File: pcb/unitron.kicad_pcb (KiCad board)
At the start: 2 copper layers, 80.5 x 141 mm, 69 parts, among them J1 Conn_01x09_Female, J2 Conn_01x09_Male, J3 Conn_01x09_Female, J4 Conn_01x09_Male, J5 Conn_02x03_Odd_Even, Q1 FDN340P, Q2 BSS123, SW1 SW_SPST, U1 LTC-4727JS, U2 LTC-4727JS, U3 AS1115-BSST, U4 ATSAMD21E, U5 LTC-4727JR, U6 LTC-4727JR, U7 AS1115-BSST

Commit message: PCB v1.5
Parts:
- removed D14: LED, LED_SMD:LED_0805_2012Metric
- removed MB1, MB2, MB3: VAL**, asl_footprints:mouse-bite-2.54mm-slot-long
- removed R2: 10KΩ, Resistor_SMD:R_0805_2012Metric
- added MB*: VAL**, asl_footprints:mouse-bite-2.54mm-slot-long, F.Cu at (72.5, 66.1)
- added MB*: VAL**, asl_footprints:mouse-bite-2.54mm-slot-long, F.Cu at (105.1, 66.1)
- added MB*: VAL**, asl_footprints:mouse-bite-2.54mm-slot-long, F.Cu at (137.4, 66.1)
- added S16: Gateron Blue, Button_Switch_Keyboard:SW_Cherry_MX_1.00u_PCB, F.Cu at (98.0, 155.2)
- added U8: AT24C01C-STUM, Package_TO_SOT_SMD:SOT-23-5, B.Cu at (121.9, 71.4)
- BT1: value 2466 -> 2468
- D1, D10, D11, D12, D2, D3, D4, D5, D6, D7, D8, D9: footprint LED_SMD:LED-APA102-2020 -> asl_footprints:LED-APA102-2020
- J1, J3: footprint Connector_PinSocket_2.54mm:PinSocket_1x09_P2.54mm_Vertical -> Connector_PinSocket_2.54mm:PinSocket_1x09_P2.54mm_Vertical_SMD_Pin1Left
- S4: footprint Button_Switch_Keyboard:SW_Cherry_MX_2.00u_PCB -> Button_Switch_Keyboard:SW_Cherry_MX_1.00u_PCB
- SW1: footprint asl_footprints:B12AP -> asl_footprints:switch_nkk_reinforced_pc_pin
- moved S4 87.4 mm to (79.0, 155.2)
- moved D10 85.4 mm to (109.6, 62.4)
- moved D11 85.4 mm to (124.0, 62.4)
- moved D12 85.4 mm to (138.3, 62.4)
- moved D4 85.4 mm to (109.6, 58.5)
- moved D5 85.4 mm to (124.0, 58.5)
- moved D6 85.4 mm to (138.3, 58.5)
- moved D1 85.4 mm to (66.6, 58.5)
- moved D2 85.4 mm to (80.9, 58.5)
- moved D7 85.4 mm to (66.6, 62.4)
- moved D8 85.4 mm to (80.9, 62.4)
- moved D3 85.4 mm to (95.3, 58.5)
- moved D9 85.4 mm to (95.3, 62.4)
- moved J3 80.9 mm to (142.2, 50.5)
- moved S15 79.5 mm to (128.3, 103.1)
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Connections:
- BT1 pad 2: (no net) -> GND
- C2 pad 2: (no net) -> GND
- D1 pad 2: (no net) -> Net-(D1-Pad2)
- D1 pad 3: (no net) -> Net-(D1-Pad3)
- D12 pad 4: /SDI -> Net-(D12-Pad4)
- D12 pad 5: /CKI -> Net-(D12-Pad5)
- D3 pad 4: Net-(D3-Pad4) -> Net-(D10-Pad3)
- D3 pad 5: Net-(D3-Pad5) -> Net-(D10-Pad2)
- D4 pad 2: Net-(D4-Pad2) -> Net-(D10-Pad5)
- D4 pad 3: Net-(D4-Pad3) -> Net-(D10-Pad4)
- D4 pad 4: Net-(D10-Pad3) -> Net-(D11-Pad3)
- D4 pad 5: Net-(D10-Pad2) -> Net-(D11-Pad2)
- D5 pad 2: Net-(D10-Pad5) -> Net-(D11-Pad5)
- D5 pad 3: Net-(D10-Pad4) -> Net-(D11-Pad4)
- D5 pad 4: Net-(D11-Pad3) -> Net-(D12-Pad3)
- D5 pad 5: Net-(D11-Pad2) -> Net-(D12-Pad2)
- D6 pad 2: Net-(D11-Pad5) -> Net-(D12-Pad5)
- D6 pad 3: Net-(D11-Pad4) -> Net-(D12-Pad4)
- D6 pad 4: Net-(D12-Pad3) -> /CKI
- D6 pad 5: Net-(D12-Pad2) -> /SDI
- D7 pad 2: Net-(D1-Pad5) -> (no net)
- D7 pad 3: Net-(D1-Pad4) -> (no net)
- D7 pad 4: Net-(D2-Pad3) -> Net-(D1-Pad3)
- D7 pad 5: Net-(D2-Pad2) -> Net-(D1-Pad2)
- D8 pad 2: Net-(D2-Pad5) -> Net-(D1-Pad5)
- D8 pad 3: Net-(D2-Pad4) -> Net-(D1-Pad4)
- D8 pad 4: Net-(D3-Pad3) -> Net-(D2-Pad3)
- D8 pad 5: Net-(D3-Pad2) -> Net-(D2-Pad2)
- D9 pad 2: Net-(D3-Pad5) -> Net-(D2-Pad5)
- D9 pad 3: Net-(D3-Pad4) -> Net-(D2-Pad4)
- D9 pad 4: Net-(D4-Pad3) -> Net-(D3-Pad3)
- D9 pad 5: Net-(D4-Pad2) -> Net-(D3-Pad2)
- J3 pad 1: /CKI -> /GND_daughter
- J3 pad 2: /SDI -> /VIN_daughter
- J3 pad 3: /GND_daughter -> /SCL
- J3 pad 4: /VIN_daughter -> /SDA
- J3 pad 5: /SCL -> Net-(J3-Pad5)
- J3 pad 6: /SDA -> Net-(J3-Pad6)
- J3 pad 7: Net-(J3-Pad7) -> /IRQ
- J3 pad 8: Net-(J3-Pad8) -> /CKI
- J3 pad 9: /IRQ -> /SDI
- J4 pad 1: /SCK -> GND
- J4 pad 2: /MOSI -> /VIN
- J4 pad 3: GND -> /SCL_mcu
- J4 pad 4: /VIN -> /SDA_mcu
- J4 pad 5: /SCL_mcu -> /KEYA
- J4 pad 6: /SDA_mcu -> /KEYB
- J4 pad 7: /KEYA -> /IRQ_mcu
- J4 pad 8: /KEYB -> /SCK
- J4 pad 9: /IRQ_mcu -> /MOSI
- U3 pad 11: Net-(J3-Pad7) -> Net-(J3-Pad5)
- U3 pad 12: Net-(J3-Pad8) -> Net-(J3-Pad6)
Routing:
- net /GND_daughter: track 92.4 -> 18.6 mm, vias 14 -> 8
- net Net-(J2-Pad7): track 57.8 -> 98.3 mm
- net Net-(J3-Pad5): track 0.00 -> 40.1 mm, vias 0 -> 2
- net Net-(J3-Pad6): track 0.00 -> 38.8 mm, vias 0 -> 2
- net /VIN_daughter: track 232.5 -> 194.7 mm, vias 5 -> 3
- net Net-(J3-Pad8): track 37.6 -> 0.00 mm, vias 2 -> 0
- net Net-(J3-Pad7): track 37.0 -> 0.00 mm, vias 1 -> 0
- net Net-(D14-Pad2): track 29.6 -> 0.00 mm, vias 1 -> 0
- net Net-(D4-Pad2): track 14.8 -> 0.00 mm
- net Net-(D4-Pad3): track 14.4 -> 0.00 mm
- net /SCK: track 47.8 -> 59.0 mm, vias 1 -> 3
- net /KEYA: track 149.4 -> 160.5 mm
- net Net-(D3-Pad3): track 14.5 -> 4.73 mm
- net Net-(D3-Pad2): track 14.8 -> 5.19 mm
- net Net-(D10-Pad4): track 14.2 -> 4.68 mm
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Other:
- board size 80.5 x 141 mm -> 80.5 x 139 mm
- board text added: "Unitron v1.5"
- board text removed: "Unitron v1.4"

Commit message: pcb v1.6
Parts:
- removed the D11 at (124.0, 62.4)
- removed D12: APA102-2020, asl_footprints:LED-APA102-2020
- added G***: LOGO, LOGO, F.Cu at (89.7, 52.0)
- added G***: LOGO, LOGO, F.Cu at (137.5, 57.8)
- added G***: LOGO, LOGO, F.Cu at (121.5, 57.8)
- added G***: LOGO, LOGO, F.Cu at (103.9, 57.8)
- added G***: LOGO, LOGO, F.Cu at (89.7, 57.8)
- added G***: LOGO, LOGO, F.Cu at (71.1, 52.1)
- added G***: LOGO, LOGO, F.Cu at (71.1, 57.8)
- added G***: LOGO, LOGO, F.Cu at (137.5, 52.0)
- added G***: LOGO, LOGO, F.Cu at (103.9, 52.0)
- added G***: LOGO, LOGO, F.Cu at (121.5, 52.0)
- added R7: 10KΩ, Resistor_SMD:R_0805_2012Metric, B.Cu at (121.5, 94.2)
- added R8: 10KΩ, Resistor_SMD:R_0805_2012Metric, B.Cu at (118.9, 94.2)
- added U1: AP2112K-3.3, Package_TO_SOT_SMD:SOT-23-5, B.Cu at (134.4, 96.6)
- BT1: footprint Battery:BatteryHolder_Keystone_2468_2xAAA -> Battery:BatteryHolder_Keystone_2479_3xAAA
- C2, C3: value 0.1µF -> 100nF
- D1, D10, D2, D3, D4, D5, D6, D7, D8, D9: value APA102-2020 -> SK9822; footprint asl_footprints:LED-APA102-2020 -> asl_footprints:LED_SK9822_5050
- J1, J3: value Conn_01x09_Female -> Conn_01x10_Male; footprint Connector_PinSocket_2.54mm:PinSocket_1x09_P2.54mm_Vertical_SMD_Pin1Left -> Connector_PinSocket_2.54mm:PinSocket_1x10_P2.54mm_Vertical_SMD_Pin1Right
- J2, J4: value Conn_01x09_Male -> Conn_01x10_Female; footprint Connector_PinHeader_2.54mm:PinHeader_1x09_P2.54mm_Vertical -> Connector_PinHeader_2.54mm:PinHeader_1x10_P2.54mm_Vertical
- moved D6 70.7 mm to (67.6, 57.8), turned to 180 degrees
- moved BT1 26.9 mm to (128.2, 94.2)
- moved D10 24.8 mm to (134.0, 57.8), turned to 180 degrees
- moved D9 23.2 mm to (118.0, 57.8), turned to 180 degrees
- moved D7 20.2 mm to (86.2, 57.8), turned to 180 degrees
- moved D8 20.0 mm to (100.4, 57.8), turned to 180 degrees
- moved D5 12.0 mm to (134.0, 52.0), turned to 180 degrees
- moved D4 10.7 mm to (118.0, 52.0), turned to 180 degrees
- moved H3 9.15 mm to (135.6, 158.0)
- moved U3 8.91 mm to (124.2, 41.4)
- moved U8 8.91 mm to (124.2, 28.3)
- moved R13 8.91 mm to (106.7, 33.4)
- moved R4 8.91 mm to (112.4, 45.6)
- moved R5 8.91 mm to (106.8, 46.1)
- moved R6 8.91 mm to (110.1, 44.5)
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- renumbered D13 to D11, R9 to R10, R10 to R11, R11 to R12, R12 to R13, R13 to R14, R14 to R15, R3 to R2, R4 to R3, R5 to R4, R6 to R5, R7 to R6, R8 to R9, S9 to S10, S10 to S11, S11 to S12, S12 to S13, S13 to S14, S14 to S15, S15 to S16, S16 to S7, S7 to S8, S8 to S9, U1 to U2, U2 to U3, U3 to U4, U4 to U5, U8 to U6, U5 to U7, U6 to U8, U7 to U9
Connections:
- D1 pad 1: /VIN_daughter -> Net-(D1-Pad1)
- D1 pad 3: Net-(D1-Pad3) -> /GND_daughter
- D1 pad 4: Net-(D1-Pad4) -> /VIN_daughter
- D1 pad 6: /GND_daughter -> Net-(D1-Pad6)
- D10 pad 1: /VIN_daughter -> Net-(D10-Pad1)
- D10 pad 3: Net-(D10-Pad3) -> /GND_daughter
- D10 pad 4: Net-(D10-Pad4) -> /VIN_daughter
- D10 pad 6: /GND_daughter -> Net-(D10-Pad6)
- D2 pad 1: /VIN_daughter -> Net-(D2-Pad1)
- D2 pad 3: Net-(D2-Pad3) -> /GND_daughter
- D2 pad 4: Net-(D2-Pad4) -> /VIN_daughter
- D2 pad 6: /GND_daughter -> Net-(D2-Pad6)
- D3 pad 1: /VIN_daughter -> Net-(D3-Pad1)
- D3 pad 3: Net-(D3-Pad3) -> /GND_daughter
- D3 pad 4: Net-(D10-Pad3) -> /VIN_daughter
- D3 pad 5: Net-(D10-Pad2) -> Net-(D3-Pad5)
- D3 pad 6: /GND_daughter -> Net-(D3-Pad6)
- D4 pad 1: /VIN_daughter -> Net-(D10-Pad6)
- D4 pad 3: Net-(D10-Pad4) -> /GND_daughter
- D4 pad 4: Net-(D11-Pad3) (its old number) -> /VIN_daughter
- D4 pad 5: Net-(D11-Pad2) -> Net-(D4-Pad5)
- D4 pad 6: /GND_daughter -> Net-(D4-Pad6)
- D5 pad 1: /VIN_daughter -> /SDI
- D5 pad 2: Net-(D11-Pad5) -> /CKI
- D5 pad 3: Net-(D11-Pad4) -> /GND_daughter
- D5 pad 4: Net-(D12-Pad3) -> /VIN_daughter
- D5 pad 5: Net-(D12-Pad2) -> Net-(D10-Pad2)
- D5 pad 6: /GND_daughter -> Net-(D10-Pad1)
- D6 pad 1: /VIN_daughter -> Net-(D1-Pad6)
- D6 pad 2: Net-(D12-Pad5) -> Net-(D1-Pad5)
- D6 pad 3: Net-(D12-Pad4) -> /GND_daughter
- D6 pad 4: /CKI -> /VIN_daughter
- D6 pad 5: /SDI -> (no net)
- D6 pad 6: /GND_daughter -> (no net)
- D7 pad 1: /VIN_daughter -> Net-(D2-Pad6)
- D7 pad 2: (no net) -> Net-(D2-Pad5)
- D7 pad 3: (no net) -> /GND_daughter
- D7 pad 4: Net-(D1-Pad3) -> /VIN_daughter
- D7 pad 6: /GND_daughter -> Net-(D1-Pad1)
- D8 pad 1: /VIN_daughter -> Net-(D3-Pad6)
- D8 pad 2: Net-(D1-Pad5) -> Net-(D3-Pad5)
- D8 pad 3: Net-(D1-Pad4) -> /GND_daughter
- D8 pad 4: Net-(D2-Pad3) -> /VIN_daughter
- D8 pad 6: /GND_daughter -> Net-(D2-Pad1)
- D9 pad 1: /VIN_daughter -> Net-(D4-Pad6)
- D9 pad 2: Net-(D2-Pad5) -> Net-(D4-Pad5)
- D9 pad 3: Net-(D2-Pad4) -> /GND_daughter
- D9 pad 4: Net-(D3-Pad3) -> /VIN_daughter
- D9 pad 6: /GND_daughter -> Net-(D3-Pad1)
- Q1 pad 3: /VIN -> Net-(Q1-Pad3)
- S7 pad 2: Net-(J2-Pad7) -> Net-(J2-Pad9)
- U5 pad 6: (no net) -> /batt_lvl
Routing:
- net Net-(J2-Pad9): track 35.2 -> 99.9 mm
- net Net-(J2-Pad7): track 98.3 -> 59.3 mm
- net /batt_lvl: track 0.00 -> 21.8 mm, vias 0 -> 2
- net Net-(D1-Pad1): track 0.00 -> 15.7 mm
- net Net-(D3-Pad1): track 0.00 -> 14.7 mm
- net Net-(D11-Pad3) (its old number): track 14.0 -> 0.00 mm
- net Net-(D2-Pad4): track 14.0 -> 0.00 mm
- net Net-(D12-Pad3): track 14.0 -> 0.00 mm
- net Net-(D12-Pad2): track 14.0 -> 0.00 mm
- net Net-(D11-Pad2): track 14.0 -> 0.00 mm
- net Net-(D10-Pad3): track 14.0 -> 0.00 mm
- net Net-(D1-Pad4): track 14.0 -> 0.00 mm
- net /GND_daughter: track 18.6 -> 4.85 mm
- net Net-(D10-Pad6): track 0.00 -> 13.1 mm
- net /VIN_daughter: track 194.7 -> 207.2 mm, vias 3 -> 5
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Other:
- board size 80.5 x 139 mm -> 80.3 x 155.9 mm
- board text added: "March 2021"
- board text added: "Unitron v1.6"
- board text removed: "C"
- board text removed: "F"
- board text removed: "Feb 2021"
- board text removed: "Unitron v1.5"
- board text removed: "ft m"
- board text removed: "in mm"
- board text removed: "lb kg"
- board text removed: "mi km"
- board text removed: "o"
- board text removed: "oz mL"

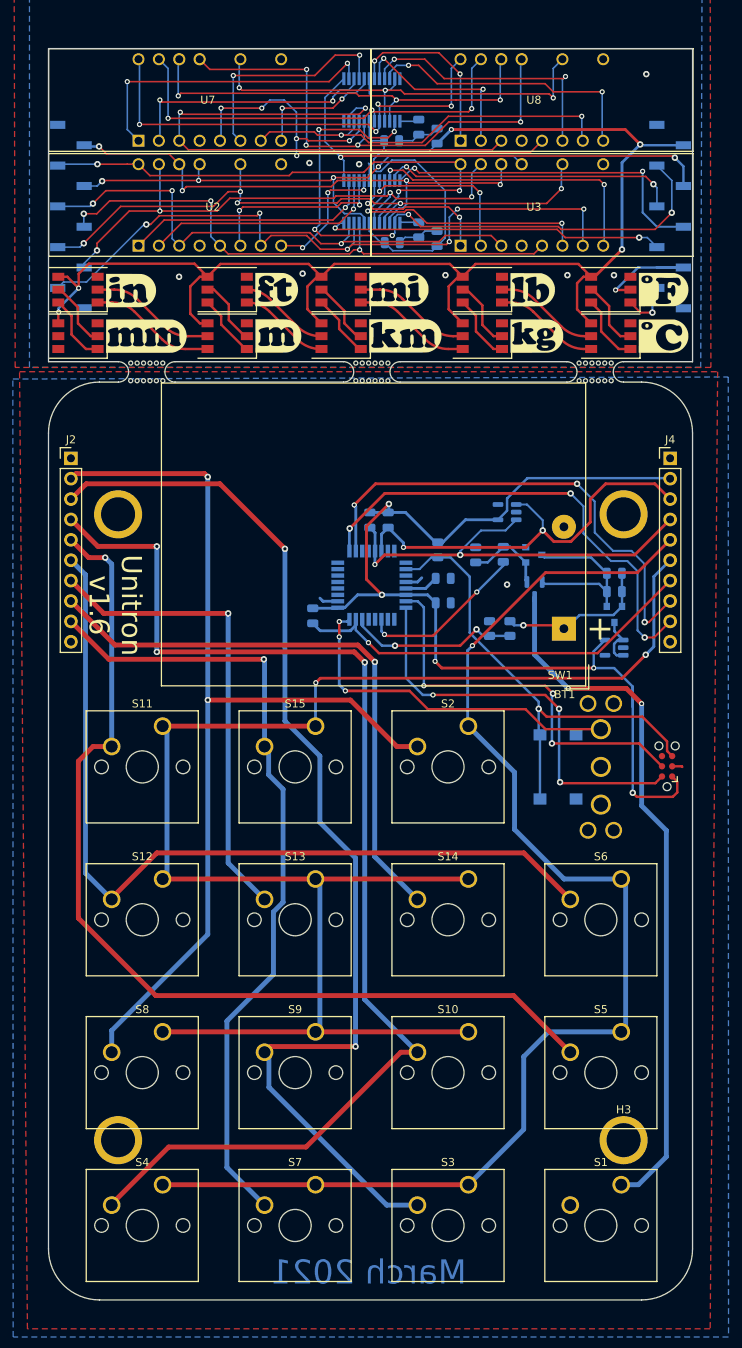
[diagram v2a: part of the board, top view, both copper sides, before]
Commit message: unitron v 1.8
changed to QT PY and added lipo battery charging circuit
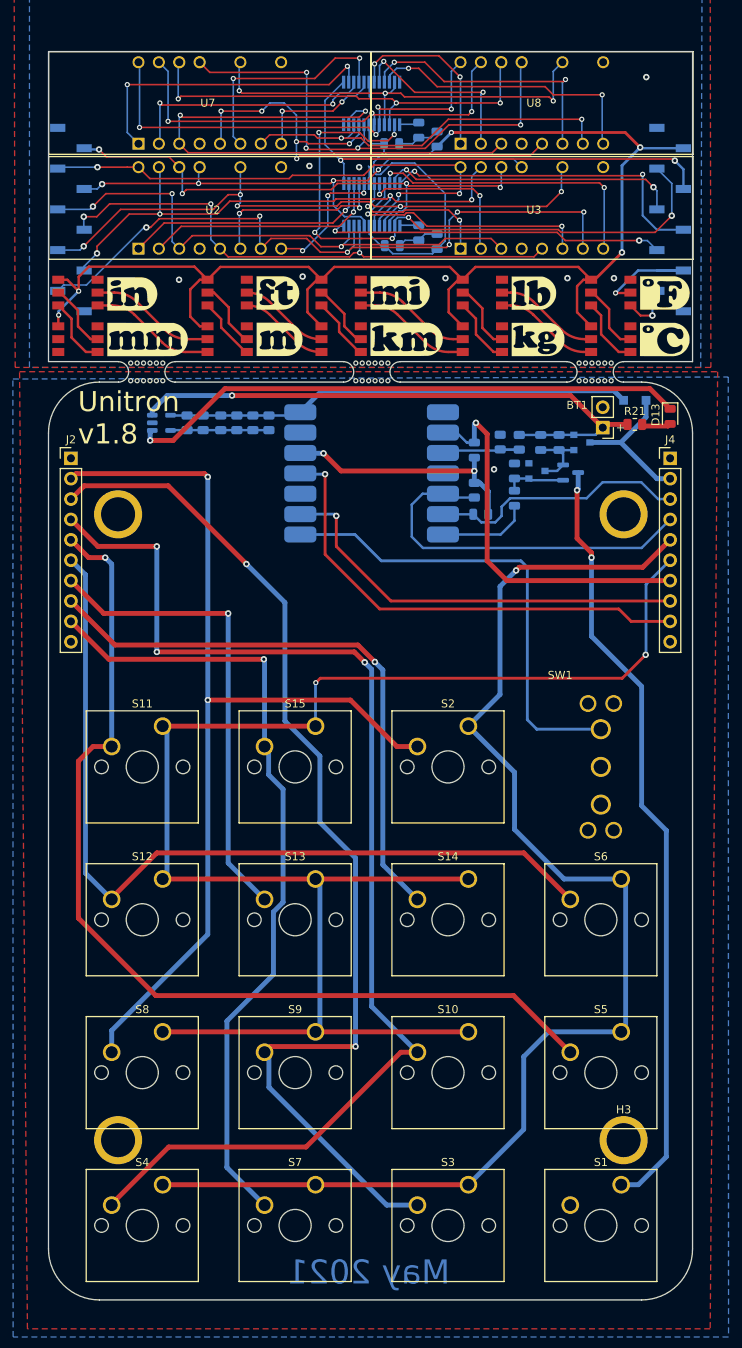
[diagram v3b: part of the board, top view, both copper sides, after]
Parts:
- removed C2, C3: 100nF, Capacitor_SMD:C_0805_2012Metric
- removed J5: Conn_02x03_Odd_Even, asl_footprints:Tag-Connect_TC2030-IDC-NL_2x03_P1.27mm_Vertical
- removed S16: B3FS-1010P, asl_footprints:6mm_tactile_smd
- removed U6: AT24C01C-STUM, Package_TO_SOT_SMD:SOT-23-5
- added D12: Diode, asl_footprints:D_SOD-123F, B.Cu at (137.0, 65.8)
- added D13: LED, LED_SMD:LED_0805_2012Metric, F.Cu at (141.4, 67.8)
- added R16: 10KΩ, Resistor_SMD:R_0805_2012Metric, B.Cu at (91.4, 68.6)
- added R17: 10KΩ, Resistor_SMD:R_0805_2012Metric, B.Cu at (87.4, 68.6)
- added R18: 10KΩ, Resistor_SMD:R_0805_2012Metric, B.Cu at (85.4, 68.6)
- added R19: 10KΩ, Resistor_SMD:R_0805_2012Metric, B.Cu at (83.2, 68.6)
- added R20: 10KΩ, Resistor_SMD:R_0805_2012Metric, B.Cu at (81.2, 68.6)
- added R21: 10KΩ, Resistor_SMD:R_0805_2012Metric, F.Cu at (137.0, 68.8)
- BT1: footprint Battery:BatteryHolder_Keystone_2479_3xAAA -> Connector_PinHeader_2.54mm:PinHeader_1x02_P2.54mm_Vertical
- U1: value AP2112K-3.3 -> MCP73831-2-OT
- U5: value ATSAMD21E -> QT_Py; footprint Package_QFP:TQFP-32_7x7mm_P0.8mm -> asl_footprints:QT_Py
- moved U1 63.0 mm to (78.0, 68.6), turned to 0 degrees
- moved R9 28.8 mm to (117.0, 72.0), turned to 90 degrees
- moved BT1 25.5 mm to (133.0, 69.2)
- moved R8 23.3 mm to (120.3, 71.0)
- moved R7 23.2 mm to (122.6, 71.0)
- moved Q1 21.8 mm to (130.4, 71.0), turned to 0 degrees
- moved C1 19.8 mm to (127.6, 71.0), turned to -90 degrees
- moved R10 18.9 mm to (89.4, 68.6), turned to -90 degrees
- moved R1 18.7 mm to (125.3, 71.0), turned to 90 degrees
- moved D11 15.2 mm to (129.0, 74.8), turned to 0 degrees
- moved U5 13.9 mm to (104.2, 74.9), turned to 180 degrees
- moved R11 11.6 mm to (117.8, 80.0), turned to 0 degrees
- moved R3 11.5 mm to (122.0, 74.6)
- moved Q2 10.5 mm to (124.8, 74.6)
- moved R15 8.71 mm to (117.0, 77.0)
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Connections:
- D6 pad 5: (no net) -> unconnected-(D6-Pad5)
- D6 pad 6: (no net) -> unconnected-(D6-Pad6)
- J1 pad 1: (no net) -> unconnected-(J1-Pad1)
- J1 pad 10: (no net) -> unconnected-(J1-Pad10)
- J2 pad 1: (no net) -> unconnected-(J2-Pad1)
- J2 pad 10: (no net) -> unconnected-(J2-Pad10)
- J3 pad 10: (no net) -> unconnected-(J3-Pad10)
- J4 pad 10: (no net) -> unconnected-(J4-Pad10)
- Q1 pad 3: Net-(Q1-Pad3) -> /VIN
- R10 pad 1: /SDA_mcu -> Net-(D12-Pad1)
- R10 pad 2: /VIN -> Net-(U1-Pad5)
- R11 pad 2: /VIN -> /3VDC
- R15 pad 1: /RST -> /SDA_mcu
- R15 pad 2: /VIN -> /3VDC
- R9 pad 1: /VIN -> /3VDC
- U1 pad 1: Net-(Q1-Pad3) -> Net-(U1-Pad1)
- U1 pad 3: Net-(Q1-Pad3) -> /VBATT
- U1 pad 4: (no net) -> Net-(D12-Pad1)
- U1 pad 5: /VIN -> Net-(U1-Pad5)
- U2 pad 4: (no net) -> unconnected-(U2-Pad4)
- U3 pad 4: (no net) -> unconnected-(U3-Pad4)
- U5 pad 1: (no net) -> unconnected-(U5-Pad1)
- U5 pad 10: GND -> unconnected-(U5-Pad10)
- U5 pad 11: (no net) -> /MOSI
- U5 pad 12: (no net) -> /3VDC
- U5 pad 13: (no net) -> GND
- U5 pad 14: (no net) -> Net-(D12-Pad1)
- U5 pad 2: (no net) -> /IRQ_mcu
- U5 pad 3: /BTN -> /batt_lvl
- U5 pad 4: (no net) -> unconnected-(U5-Pad4)
- U5 pad 5: (no net) -> /SDA_mcu
- U5 pad 6: /batt_lvl -> /SCL_mcu
- U5 pad 7: /IRQ_mcu -> /BTN
- U5 pad 9: /VIN -> /SCK
- U7 pad 4: (no net) -> unconnected-(U7-Pad4)
- U8 pad 4: (no net) -> unconnected-(U8-Pad4)
- U9 pad 12: (no net) -> unconnected-(U9-Pad12)
- U9 pad 24: (no net) -> unconnected-(U9-Pad24)
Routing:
- net /VIN: track 135.5 -> 18.4 mm, vias 5 -> 0
- net Net-(U1-Pad1): track 0.00 -> 69.9 mm, vias 0 -> 1
- net /RST: track 60.7 -> 0.00 mm, vias 1 -> 0
- net Net-(D12-Pad1): track 0.00 -> 58.3 mm
- net /VBATT: track 20.6 -> 73.6 mm
- net /SWDIO: track 51.7 -> 0.00 mm, vias 3 -> 0
- net /SWCLK: track 50.0 -> 0.00 mm, vias 3 -> 0
- net /3VDC: track 0.00 -> 30.8 mm, vias 0 -> 2
- net /SCL_mcu: track 52.1 -> 32.4 mm, vias 2 -> 0
- net /mode: track 45.1 -> 58.6 mm, vias 3 -> 0
- net Net-(C1-Pad2): track 21.8 -> 8.98 mm
- net Net-(U1-Pad5): track 0.00 -> 12.3 mm
- net /batt_lvl: track 21.8 -> 9.71 mm, vias 2 -> 0
- net /BTN: track 21.0 -> 11.5 mm, vias 2 -> 0
- net Net-(D11-Pad3): track 87.8 -> 97.0 mm
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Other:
- board size 80.3 x 155.9 mm -> 80.3 x 155.6 mm
- board text added: "+"
- board text added: "May 2021"
- board text added: "Unitron v1.8"
- board text removed: "March 2021"
- board text removed: "Unitron v1.6"
